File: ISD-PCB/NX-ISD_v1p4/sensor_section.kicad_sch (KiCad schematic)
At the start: 33 parts, among them U10 OPT3001DNPR, U11 BNO085, U12 RV-3028-C7, U6 MAX17048G_T10, U7 BME690, U8 MAX30102, U9 PCA9306, Y1 32.768 kHz

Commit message: feat(pcb): v1.4 schematic and layout updates for 4-bit SDMMC, direct display SPI, and button pullups
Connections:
- net !INT_ALS: no longer names the net of U10.5 (INT)
- net !INT_H renamed !INT_DOF
- no-connect marks 1 -> 2
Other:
- note added: "NOTE: !INT_ALS IS NOT CONNECTED. THIS IS DUE TO THE LACK OF A SERIOUS FUNCTIONAL ADVANTAGE."
- moved on the sheet: C18, U10

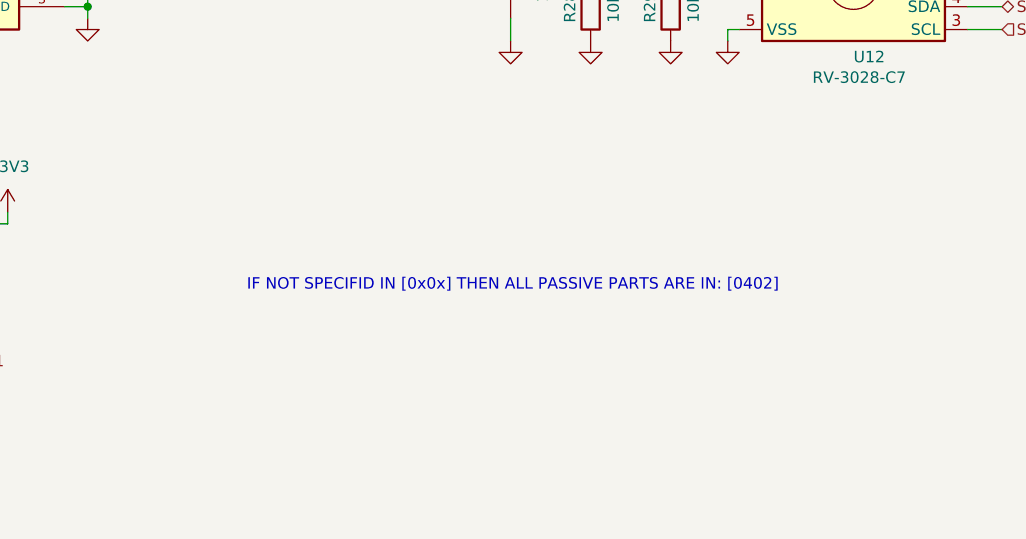
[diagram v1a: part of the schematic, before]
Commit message: hw(v1.4): bq25170 thermal optimization, usb-c plating, battery pad stitching, and npm decoupling
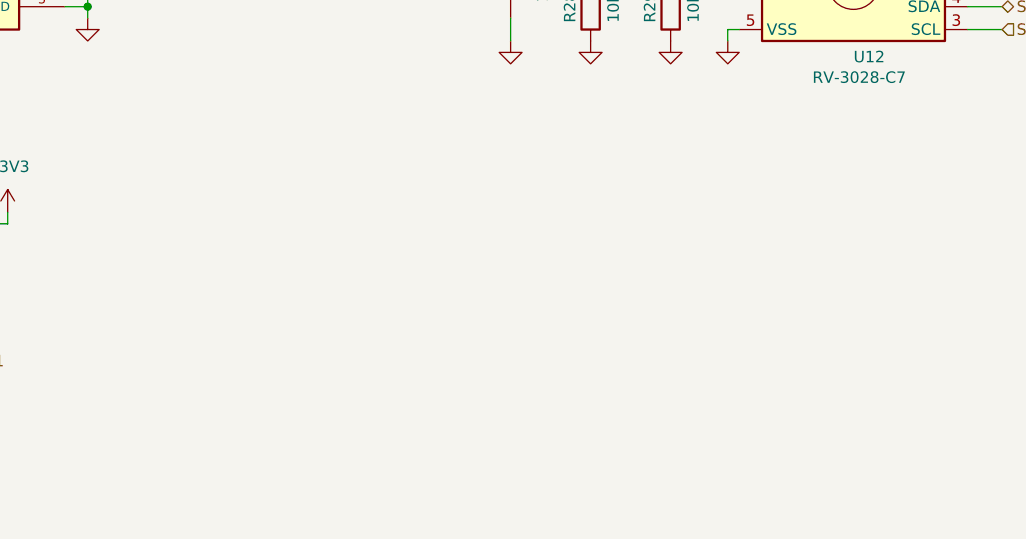
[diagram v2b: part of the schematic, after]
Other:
- note removed: "IF NOT SPECIFID IN [0x0x] THEN ALL PASSIVE PARTS ARE IN: [0402]"
- title: (none) -> NX-ISD Version 1 Rev. 4
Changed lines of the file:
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@@
 	(generator_version "10.0")
 	(paper "A4")
-	(text "IF NOT SPECIFID IN [0x0x] THEN ALL PASSIVE PARTS ARE IN: [0402]"
-		(exclude_from_sim no)
-		(at 211.074 168.148 0)
-		(effects
-			(font
-				(size 1.27 1.27)
-			)
-		)
+	(title_block
+		(title "NX-ISD Version 1 Rev. 4")
+		(date "2026-10-16")
+		(rev "p4")
+		(comment 1 "IF NOT SPECIFID IN [0x0x] THEN ALL PASSIVE PARTS ARE IN: [0402]")
 	)
 	(text "[0603]"

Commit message: hw(v1p4): add RTC backup supercap C27, tactile buttons, USBLC6 footprint adjustments, and cyberpunk silkscreens
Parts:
- removed R28: 10k, Resistor_SMD:R_0402_1005Metric, symbol Device:R
- added C5: CPH3225A, NX-AW-footprints:CAPCP3225X100N, symbol CPH3225A:CPH3225A
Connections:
- net GND: now also C5.2
- net at U12.6 (VBACKUP): now also C5.1
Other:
- moved on the sheet: C20
